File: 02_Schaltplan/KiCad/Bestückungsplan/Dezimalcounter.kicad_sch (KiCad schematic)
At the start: 27 parts, among them Q11 BC858, SW1 START, U1 74HC08PW, U2 74HC02PW, U28 74HC1G126, U3 74AHC1G32, U32 74AHC1G14, U5 CD74HC4514M96, U6 SN74LS93

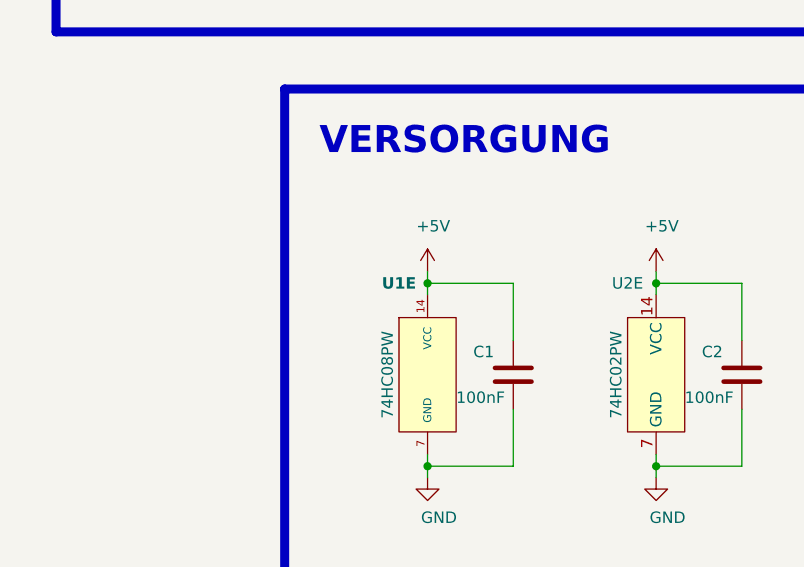
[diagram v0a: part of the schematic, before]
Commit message: Changes & ADD
+Bestückungsplan
+Auftragsplannung
@ Klärung verschiedener Begrifflichkeiten
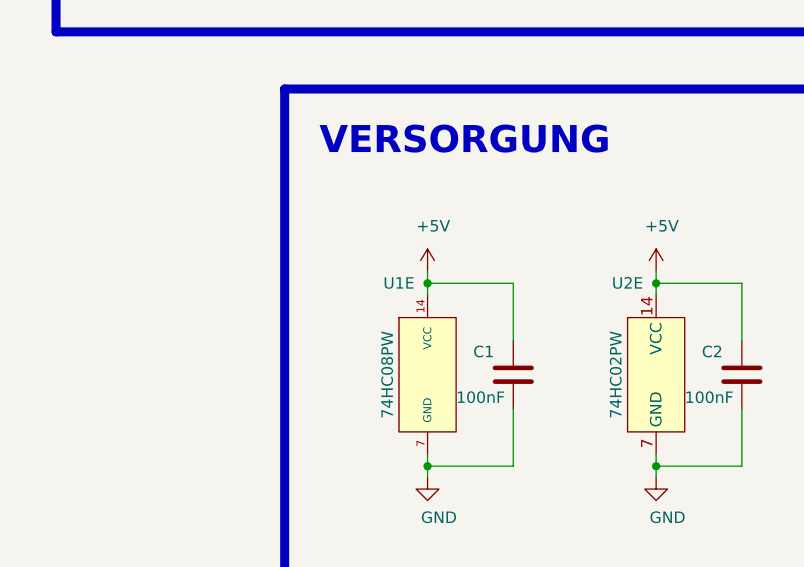
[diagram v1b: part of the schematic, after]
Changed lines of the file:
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@@
   (symbol (lib_id "Kabeltester:74HC08PW") (at 60.325 247.65 0) (unit 5)
     (in_bom yes) (on_board yes)
-    (property "Reference" "U1" (id 0) (at 57.15 237.49 0)
-      (effects (font (size 1.27 1.27) bold))
-    )
+    (property "Reference" "U1" (id 0) (at 57.15 237.49 0))
     (property "Value" "74HC08PW" (id 1) (at 55.88 247.65 90))
     (property "Footprint" "Package_SO:TSSOP-14_4.4x5mm_P0.65mm" (id 2) (at 66.675 262.89 0)
